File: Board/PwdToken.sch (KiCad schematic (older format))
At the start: 12 parts, among them J1 USB_A_PCB, J2 JST_6_PIN_VERTICAL, SW1 A, SW2 B, U1 ATtiny85-20SU

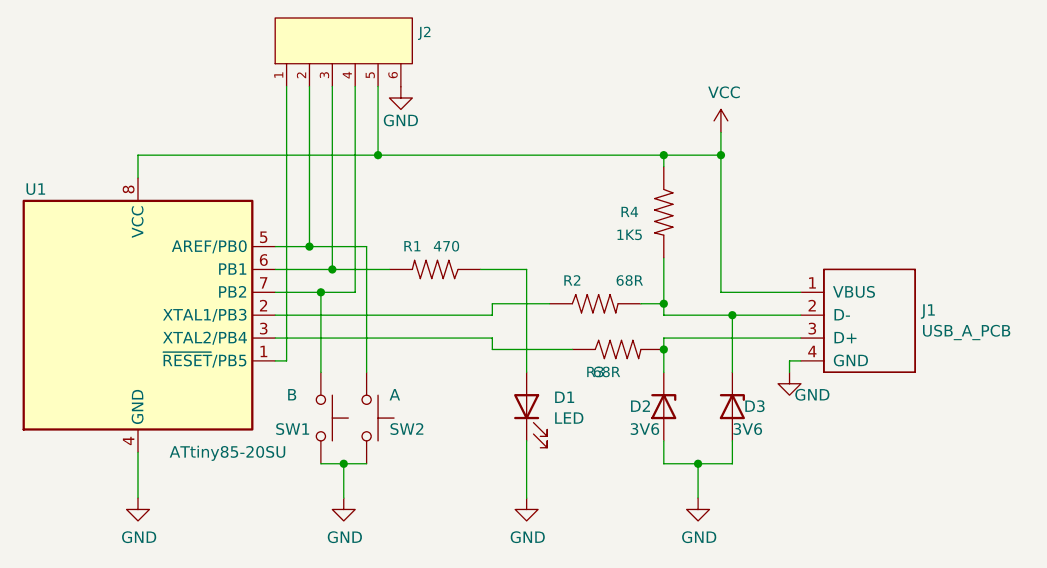
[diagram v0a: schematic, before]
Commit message: Add schematic
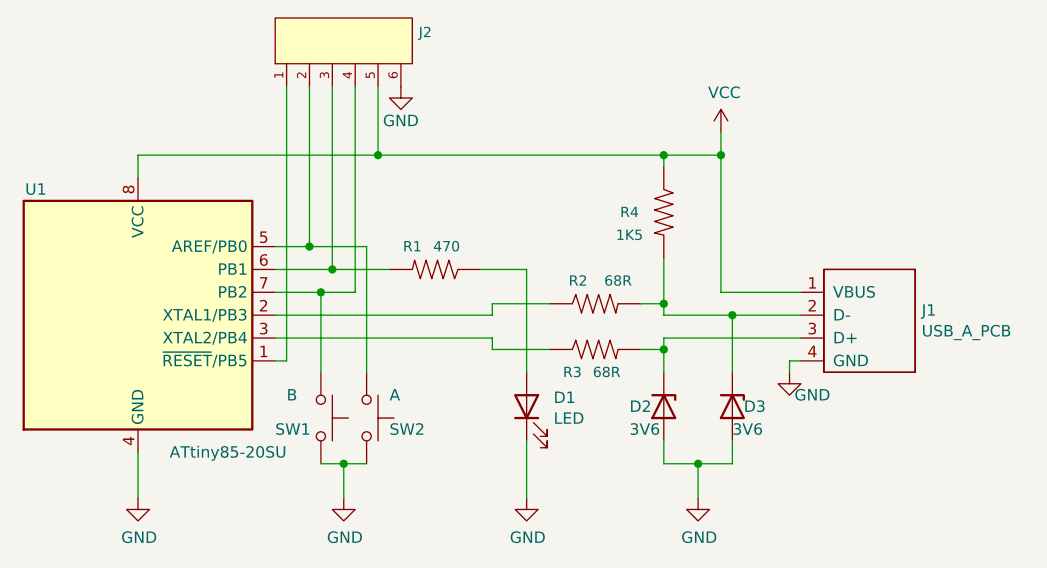
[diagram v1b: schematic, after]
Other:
- moved on the sheet: R3
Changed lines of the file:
@@
 U 1 1 60856623
 P 5450 3400
-F 0 "R2" H 5350 3500 45  0000 C CNN
-F 1 "68R" H 5500 3100 45  0000 C CNN
+F 0 "R2" H 5375 3500 45  0000 C CNN
+F 1 "68R" H 5550 3500 45  0000 C CNN
 F 2 "Resistor_SMD:R_0805_2012Metric_Pad1.20x1.40mm_HandSolder" H 5450 3550 20  0001 C CNN
 F 3 "" H 5450 3400 60  0001 C CNN
@@
 L SparkFun-Resistors:RESISTOR0402 R3
 U 1 1 60858241
-P 5550 3600
-F 0 "R3" H 5450 3500 45  0000 C CNN
-F 1 "68R" H 5600 3900 45  0000 C CNN
-F 2 "Resistor_SMD:R_0805_2012Metric_Pad1.20x1.40mm_HandSolder" H 5550 3750 20  0001 C CNN
-F 3 "" H 5550 3600 60  0001 C CNN
-F 4 " " H 5550 3721 60  0000 C CNN "Field4"
-	1    5550 3600
+P 5450 3600
+F 0 "R3" H 5350 3500 45  0000 C CNN
+F 1 "68R" H 5500 3500 45  0000 C CNN
+F 2 "Resistor_SMD:R_0805_2012Metric_Pad1.20x1.40mm_HandSolder" H 5450 3750 20  0001 C CNN
+F 3 "" H 5450 3600 60  0001 C CNN
+F 4 " " H 5450 3721 60  0000 C CNN "Field4"
+	1    5450 3600
 	1    0    0    -1
 $EndComp
@@
 	5000 3550 5000 3600
 Wire Wire Line
-	5000 3600 5350 3600
-Wire Wire Line
-	5750 3600 5750 3550
+	5000 3600 5250 3600
 $Comp
 L power:VCC #PWR05
@@
 $EndComp
 Wire Wire Line
-	5750 3550 6350 3550
-Wire Wire Line
 	5750 3450 6050 3450
 Wire Wire Line
@@
 Wire Wire Line
 	5750 4100 5900 4100
-Wire Wire Line
-	5750 3700 5750 3600
-Connection ~ 5750 3600
 Wire Wire Line
 	6050 3700 6050 3450
@@
 Wire Wire Line
 	5750 3400 5750 3450
+Wire Wire Line
+	5750 3700 5750 3600
+Wire Wire Line
+	5750 3550 6350 3550
+Wire Wire Line
+	5650 3600 5750 3600
+Connection ~ 5750 3600
+Wire Wire Line
+	5750 3600 5750 3550
 $EndSCHEMATC
